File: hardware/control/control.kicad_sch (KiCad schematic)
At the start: 59 parts, among them J1 Conn_01x05_Male, J2 DCDC-PWM, J3 display, J4 DCDC-MEASURES, J5 CANPWR, J6 CANGND, J7 RJ45, J8 RJ45, J9 Conn_02x03_Odd_Even, Q1 BSS123, SW1 next, SW2 select, U1 2.048V, U2 AP63200WU, U3 PIC18F27Q84, U4 TLE9250VSJXUMA1, Y1 10Mhz

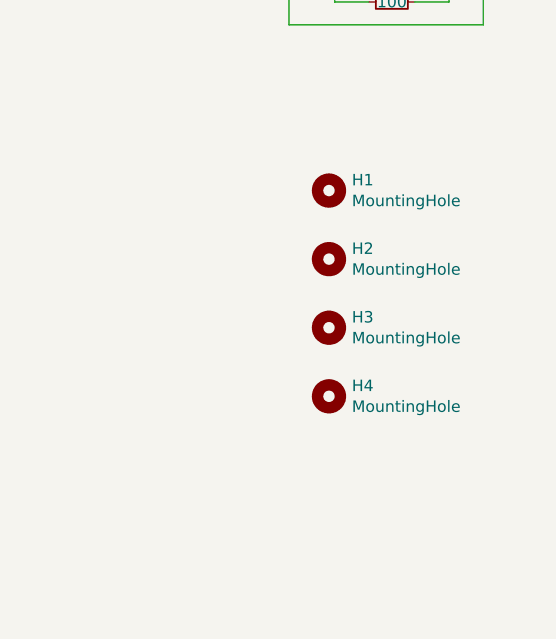
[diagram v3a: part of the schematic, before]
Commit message: Connect mounting holes to GND
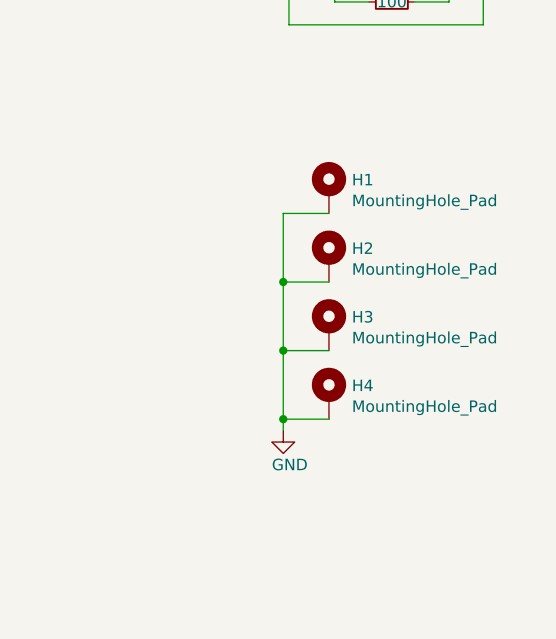
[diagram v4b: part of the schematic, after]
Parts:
- H1, H2, H3, H4: value MountingHole -> MountingHole_Pad; footprint MountingHole:MountingHole_3.2mm_M3_DIN965 -> MountingHole:MountingHole_3.2mm_M3_DIN965_Pad; symbol Mechanical:MountingHole -> Mechanical:MountingHole_Pad
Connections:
- net GND: now also H1.1, H2.1, H3.1, H4.1
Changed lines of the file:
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@@
   (junction (at 201.93 49.53) (diameter 0) (color 0 0 0 0)
   )
+  (junction (at 249.555 106.045) (diameter 0) (color 0 0 0 0)
+  )
   (junction (at 58.42 85.09) (diameter 0) (color 0 0 0 0)
   )
@@
   (junction (at 24.13 155.575) (diameter 0) (color 0 0 0 0)
   )
+  (junction (at 249.555 113.665) (diameter 0) (color 0 0 0 0)
+  )
   (junction (at 58.42 87.63) (diameter 0) (color 0 0 0 0)
   )
@@
   )
   (junction (at 69.85 155.575) (diameter 0) (color 0 0 0 0)
+  )
+  (junction (at 249.555 98.425) (diameter 0) (color 0 0 0 0)
   )
   (junction (at 186.69 57.15) (diameter 0) (color 0 0 0 0)
@@
     (stroke (width 0) (type default) (color 0 0 0 0))
   )
+  (wire (pts (xy 249.555 106.045) (xy 249.555 98.425))
+    (stroke (width 0) (type default) (color 0 0 0 0))
+  )
   (wire (pts (xy 146.05 100.33) (xy 148.59 100.33))
     (stroke (width 0) (type default) (color 0 0 0 0))
@@
     (stroke (width 0) (type default) (color 0 0 0 0))
   )
+  (wire (pts (xy 249.555 113.665) (xy 254.635 113.665))
+    (stroke (width 0) (type default) (color 0 0 0 0))
+  )
   (wire (pts (xy 69.85 163.195) (xy 69.85 164.465))
     (stroke (width 0) (type default) (color 0 0 0 0))
@@
     (stroke (width 0) (type default) (color 0 0 0 0))
   )
+  (wire (pts (xy 249.555 90.805) (xy 254.635 90.805))
+    (stroke (width 0) (type default) (color 0 0 0 0))
+  )
   (wire (pts (xy 160.02 59.69) (xy 160.02 57.15))
     (stroke (width 0) (type default) (color 0 0 0 0))
@@
     (stroke (width 0) (type default) (color 0 0 0 0))
   )
+  (wire (pts (xy 249.555 113.665) (xy 249.555 106.045))
+    (stroke (width 0) (type default) (color 0 0 0 0))
+  )
   (wire (pts (xy 100.33 26.67) (xy 101.6 26.67))
     (stroke (width 0) (type default) (color 0 0 0 0))
@@
     (stroke (width 0) (type default) (color 0 0 0 0))
   )
+  (wire (pts (xy 249.555 98.425) (xy 254.635 98.425))
+    (stroke (width 0) (type default) (color 0 0 0 0))
+  )
   (wire (pts (xy 90.17 155.575) (xy 90.17 156.845))
     (stroke (width 0) (type default) (color 0 0 0 0))
@@
     (stroke (width 0) (type default) (color 0 0 0 0))
   )
+  (wire (pts (xy 249.555 98.425) (xy 249.555 90.805))
+    (stroke (width 0) (type default) (color 0 0 0 0))
+  )
   (wire (pts (xy 134.62 77.47) (xy 101.6 77.47))
     (stroke (width 0) (type default) (color 0 0 0 0))
@@
     (stroke (width 0) (type default) (color 0 0 0 0))
   )
+  (wire (pts (xy 249.555 106.045) (xy 254.635 106.045))
+    (stroke (width 0) (type default) (color 0 0 0 0))
+  )
   (wire (pts (xy 62.23 155.575) (xy 62.23 158.115))
     (stroke (width 0) (type default) (color 0 0 0 0))
@@
   )
   (wire (pts (xy 60.96 85.09) (xy 58.42 85.09))
+    (stroke (width 0) (type default) (color 0 0 0 0))
+  )
+  (wire (pts (xy 249.555 114.935) (xy 249.555 113.665))
     (stroke (width 0) (type default) (color 0 0 0 0))
   )
@@
     (effects (font (size 1.27 1.27)) (justify right))
   )
-  (symbol (lib_id "Mechanical:MountingHole") (at 254.635 88.265 0) (unit 1)
+  (symbol (lib_id "Mechanical:MountingHole_Pad") (at 254.635 88.265 0) (unit 1)
     (in_bom yes) (on_board yes)
     (property "Reference" "H1" (id 0) (at 257.175 87.0966 0)
       (effects (font (size 1.27 1.27)) (justify left))
     )
-    (property "Value" "MountingHole" (id 1) (at 257.175 89.408 0)
-      (effects (font (size 1.27 1.27)) (justify left))
-    )
-    (property "Footprint" "MountingHole:MountingHole_3.2mm_M3_DIN965" (id 2) (at 254.635 88.265 0)
+    (property "Value" "MountingHole_Pad" (id 1) (at 257.175 89.408 0)
+      (effects (font (size 1.27 1.27)) (justify left))
+    )
+    (property "Footprint" "MountingHole:MountingHole_3.2mm_M3_DIN965_Pad" (id 2) (at 254.635 88.265 0)
       (effects (font (size 1.27 1.27)) hide)
     )
@@
       (effects (font (size 1.27 1.27)) hide)
     )
-  )
-  (symbol (lib_id "Mechanical:MountingHole") (at 254.635 95.885 0) (unit 1)
+    (pin "1")
+  )
+  (symbol (lib_id "Mechanical:MountingHole_Pad") (at 254.635 95.885 0) (unit 1)
     (in_bom yes) (on_board yes)
     (property "Reference" "H2" (id 0) (at 257.175 94.7166 0)
       (effects (font (size 1.27 1.27)) (justify left))
     )
-    (property "Value" "MountingHole" (id 1) (at 257.175 97.028 0)
-      (effects (font (size 1.27 1.27)) (justify left))
-    )
-    (property "Footprint" "MountingHole:MountingHole_3.2mm_M3_DIN965" (id 2) (at 254.635 95.885 0)
+    (property "Value" "MountingHole_Pad" (id 1) (at 257.175 97.028 0)
+      (effects (font (size 1.27 1.27)) (justify left))
+    )
+    (property "Footprint" "MountingHole:MountingHole_3.2mm_M3_DIN965_Pad" (id 2) (at 254.635 95.885 0)
       (effects (font (size 1.27 1.27)) hide)
     )
@@
       (effects (font (size 1.27 1.27)) hide)
     )
-  )
-  (symbol (lib_id "Mechanical:MountingHole") (at 254.635 103.505 0) (unit 1)
+    (pin "1")
+  )
+  (symbol (lib_id "Mechanical:MountingHole_Pad") (at 254.635 103.505 0) (unit 1)
     (in_bom yes) (on_board yes)
     (property "Reference" "H3" (id 0) (at 257.175 102.3366 0)
       (effects (font (size 1.27 1.27)) (justify left))
     )
-    (property "Value" "MountingHole" (id 1) (at 257.175 104.648 0)
-      (effects (font (size 1.27 1.27)) (justify left))
-    )
-    (property "Footprint" "MountingHole:MountingHole_3.2mm_M3_DIN965" (id 2) (at 254.635 103.505 0)
+    (property "Value" "MountingHole_Pad" (id 1) (at 257.175 104.648 0)
+      (effects (font (size 1.27 1.27)) (justify left))
+    )
+    (property "Footprint" "MountingHole:MountingHole_3.2mm_M3_DIN965_Pad" (id 2) (at 254.635 103.505 0)
       (effects (font (size 1.27 1.27)) hide)
     )
@@
       (effects (font (size 1.27 1.27)) hide)
     )
-  )
-  (symbol (lib_id "Mechanical:MountingHole") (at 254.635 111.125 0) (unit 1)
+    (pin "1")
+  )
+  (symbol (lib_id "Mechanical:MountingHole_Pad") (at 254.635 111.125 0) (unit 1)
     (in_bom yes) (on_board yes)
     (property "Reference" "H4" (id 0) (at 257.175 109.9566 0)
       (effects (font (size 1.27 1.27)) (justify left))
     )
-    (property "Value" "MountingHole" (id 1) (at 257.175 112.268 0)
-      (effects (font (size 1.27 1.27)) (justify left))
-    )
-    (property "Footprint" "MountingHole:MountingHole_3.2mm_M3_DIN965" (id 2) (at 254.635 111.125 0)
+    (property "Value" "MountingHole_Pad" (id 1) (at 257.175 112.268 0)
+      (effects (font (size 1.27 1.27)) (justify left))
+    )
+    (property "Footprint" "MountingHole:MountingHole_3.2mm_M3_DIN965_Pad" (id 2) (at 254.635 111.125 0)
       (effects (font (size 1.27 1.27)) hide)
     )
@@
       (effects (font (size 1.27 1.27)) hide)
     )
+    (pin "1")
   )
   (symbol (lib_id "Device:C_Small") (at 36.83 54.61 180) (unit 1)
@@
     (pin "2")
   )
+  (symbol (lib_id "power:GND") (at 249.555 114.935 0) (unit 1)
+    (in_bom yes) (on_board yes)
+    (property "Reference" "#PWR0101" (id 0) (at 249.555 121.285 0)
+      (effects (font (size 1.27 1.27)) hide)
+    )
+    (property "Value" "GND" (id 1) (at 248.285 118.745 0)
+      (effects (font (size 1.27 1.27)) (justify left))
+    )
+    (property "Footprint" "" (id 2) (at 249.555 114.935 0)
+      (effects (font (size 1.27 1.27)) hide)
+    )
+    (property "Datasheet" "" (id 3) (at 249.555 114.935 0)
+      (effects (font (size 1.27 1.27)) hide)
+    )
+    (pin "1")
+  )
   (symbol (lib_id "power:GND") (at 138.43 144.78 270) (unit 1)
     (in_bom yes) (on_board yes)
@@
       (reference "#PWR025") (unit 1) (value "GND") (footprint "")
     )
+    (path "/e44adf41-b30e-4095-bd13-bd9bebc6ff54"
+      (reference "#PWR0101") (unit 1) (value "GND") (footprint "")
+    )
     (path "/0c0222ff-2875-415e-9bf8-78a11b090087"
       (reference "C1") (unit 1) (value "100nF") (footprint "Capacitor_SMD:C_0603_1608Metric_Pad1.08x0.95mm_HandSolder")
@@
     )
     (path "/00000000-0000-0000-0000-000061a7b063"
-      (reference "H1") (unit 1) (value "MountingHole") (footprint "MountingHole:MountingHole_3.2mm_M3_DIN965")
+      (reference "H1") (unit 1) (value "MountingHole_Pad") (footprint "MountingHole:MountingHole_3.2mm_M3_DIN965_Pad")
     )
     (path "/00000000-0000-0000-0000-000061a7b8ca"
-      (reference "H2") (unit 1) (value "MountingHole") (footprint "MountingHole:MountingHole_3.2mm_M3_DIN965")
+      (reference "H2") (unit 1) (value "MountingHole_Pad") (footprint "MountingHole:MountingHole_3.2mm_M3_DIN965_Pad")
     )
     (path "/00000000-0000-0000-0000-000061a7c080"
-      (reference "H3") (unit 1) (value "MountingHole") (footprint "MountingHole:MountingHole_3.2mm_M3_DIN965")
+      (reference "H3") (unit 1) (value "MountingHole_Pad") (footprint "MountingHole:MountingHole_3.2mm_M3_DIN965_Pad")
     )
     (path "/00000000-0000-0000-0000-000061a7c83e"
-      (reference "H4") (unit 1) (value "MountingHole") (footprint "MountingHole:MountingHole_3.2mm_M3_DIN965")
+      (reference "H4") (unit 1) (value "MountingHole_Pad") (footprint "MountingHole:MountingHole_3.2mm_M3_DIN965_Pad")
     )
     (path "/2f9ee5b6-ea05-4a48-b884-75b3a992d209"

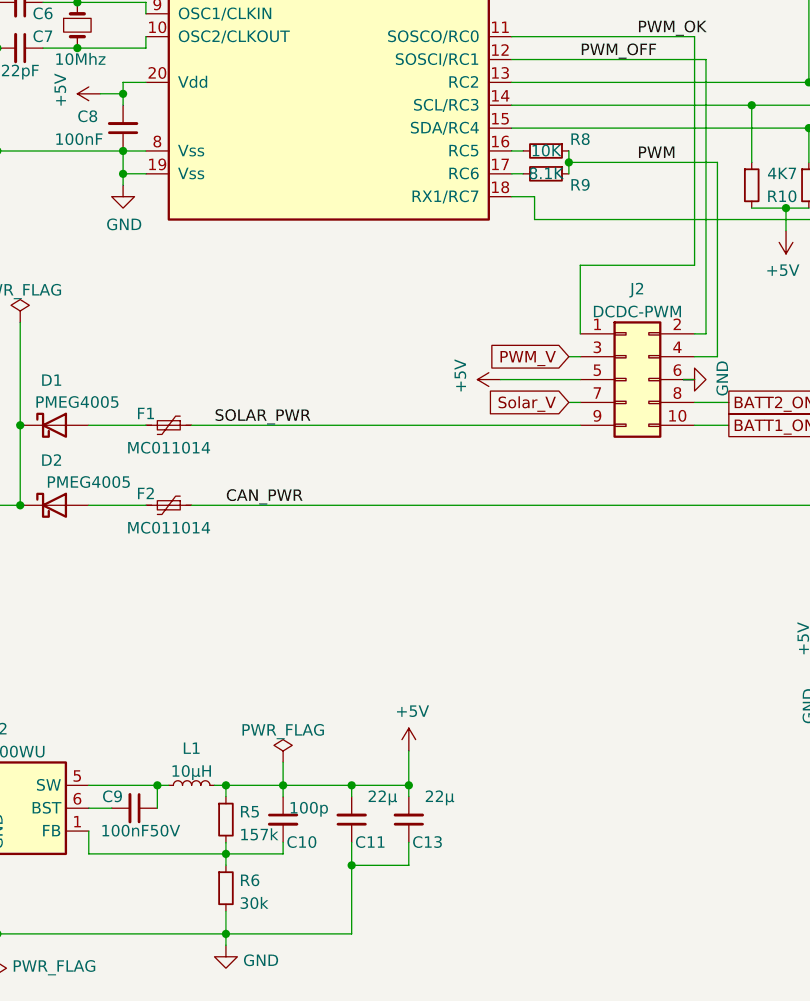
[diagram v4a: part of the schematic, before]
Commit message: Change some resistor values to match available ones.
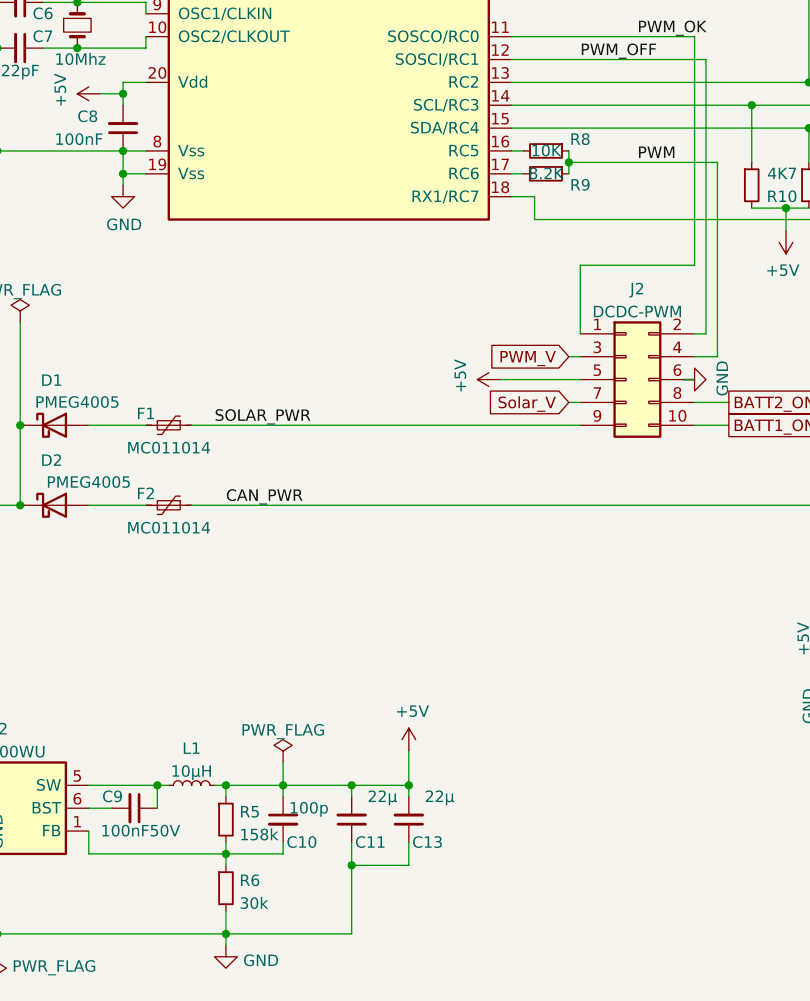
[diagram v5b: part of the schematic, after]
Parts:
- R5: value 157k -> 158k
- R9: value 8.1K -> 8.2K
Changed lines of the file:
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@@
       (effects (font (size 1.27 1.27)) (justify left))
     )
-    (property "Value" "157k" (id 1) (at 71.3486 161.0872 0)
+    (property "Value" "158k" (id 1) (at 71.3486 161.0872 0)
       (effects (font (size 1.27 1.27)) (justify left))
     )
@@
     (in_bom yes) (on_board yes)
     (property "Reference" "R9" (id 0) (at 109.22 88.9 90))
-    (property "Value" "8.1K" (id 1) (at 105.41 87.63 90))
+    (property "Value" "8.2K" (id 1) (at 105.41 87.63 90))
     (property "Footprint" "Resistor_THT:R_Axial_DIN0309_L9.0mm_D3.2mm_P12.70mm_Horizontal" (id 2) (at 105.41 87.63 0)
       (effects (font (size 1.27 1.27)) hide)
@@
     )
     (path "/479b96ca-fb1f-42d0-a461-dd1ffdaa48ed"
-      (reference "R5") (unit 1) (value "157k") (footprint "Resistor_SMD:R_0805_2012Metric_Pad1.20x1.40mm_HandSolder")
+      (reference "R5") (unit 1) (value "158k") (footprint "Resistor_SMD:R_0805_2012Metric_Pad1.20x1.40mm_HandSolder")
     )
     (path "/108067c9-3b07-4717-981c-4291820aa245"
@@
     )
     (path "/c828a5e3-fc2a-4595-959c-e2638d431d51"
-      (reference "R9") (unit 1) (value "8.1K") (footprint "Resistor_THT:R_Axial_DIN0309_L9.0mm_D3.2mm_P12.70mm_Horizontal")
+      (reference "R9") (unit 1) (value "8.2K") (footprint "Resistor_THT:R_Axial_DIN0309_L9.0mm_D3.2mm_P12.70mm_Horizontal")
     )
     (path "/0b89861b-d684-4581-aab7-bfb40d7ac71f"
